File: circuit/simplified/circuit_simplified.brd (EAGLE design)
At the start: 100 x 80 mm, 78 parts

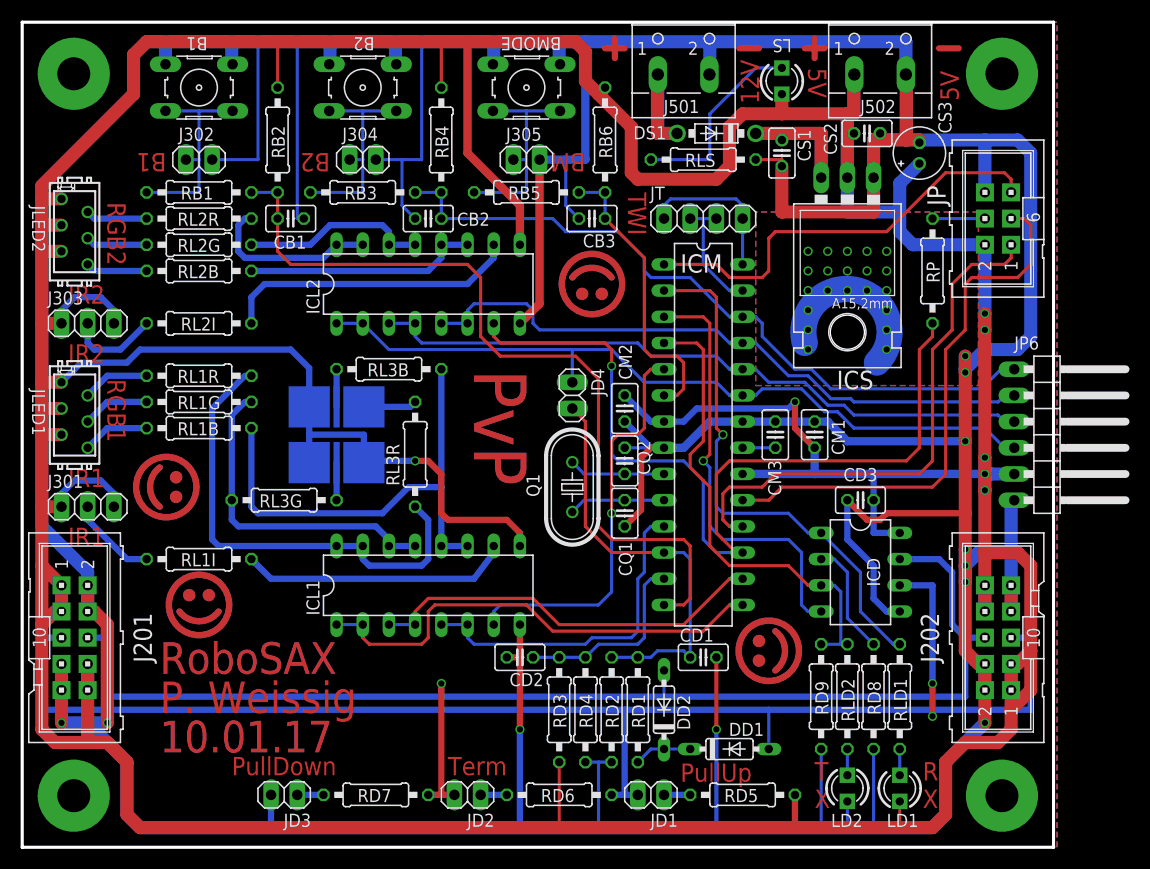
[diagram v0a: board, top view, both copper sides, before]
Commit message: updated circuit (added simplified version & minor bugfixes)
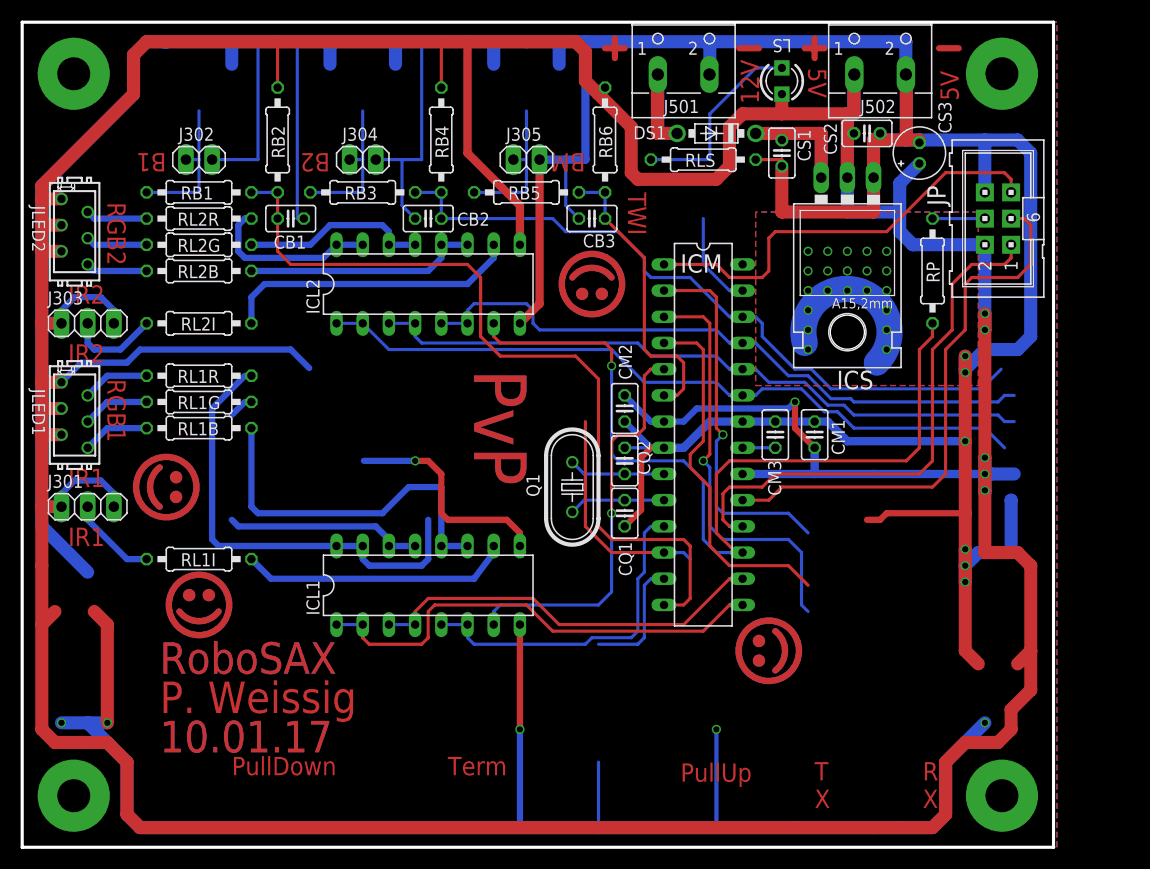
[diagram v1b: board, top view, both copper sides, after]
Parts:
- removed B1, B2, BMODE: (no value), switch-omron:B3F-10XX
- removed CD1, CD2: 100pF, rcl:C025-025X050
- removed CD3: 100nF, rcl:C025-025X050
- removed DD1, DD2: 1N4148, diode:DO35-7
- removed ICD: DRIVER_RS485, robo_ag:IC_DIL08
- removed J201, J202: (no value), robo_ag:STECKER_WANNE_10
- removed JD1, JD2, JD3, JD4: (no value), pinhead:1X02
- removed JP6: (no value), pinhead:1X06/90
- removed JT: (no value), pinhead:1X04
- removed LD1, LD2: (no value), robo_ag:LED_3MM
- removed LED3: LED_3X, robo_ag:LED_TOP_PLCC6
- removed RD1, RD6: 150, rcl:0207/10
- removed RD2: 100k, rcl:0207/10
- removed RD3, RD4: ?, rcl:0207/10
- removed RD5, RD7: 1k, rcl:0207/10
- removed RD8, RD9: 10k, rcl:0207/10
- removed RL3B, RL3G: 22, rcl:0207/10
- removed RL3R: 40,4, rcl:0207/10
- removed RLD1, RLD2: 300, rcl:0207/10
- LS: value (none) -> red
- RLS: value 300 -> 2k
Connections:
- removed net BUS_A: DD1.A, ICD.6, J201.5, J202.5, JD1.2, RD6.2
- removed net BUS_B: DD2.A, ICD.7, J201.6, J202.6, JD2.2, RD7.2
- removed net N$24: LED3.6, RL3R.2
- removed net N$25: LED3.2, RL3G.2
- removed net N$26: LED3.5, RL3B.2
- removed net N$31: JD1.1, RD5.1
- removed net N$32: ICD.2, RD8.1
- removed net N$33: JD2.1, RD6.1
- removed net N$34: LD1.K, RLD1.1
- removed net N$35: JD3.1, RD7.1
- removed net N$36: DD1.C, DD2.C, RD1.1
- removed net N$37: LD2.A, RLD2.2
- net +5V: no longer CD3.1, ICD.8, J201.1, J201.10, J201.3, J201.8, J202.1, J202.10, J202.3, J202.8, JP6.5, LD1.A, LED3.1, LED3.3, LED3.4, RD3.1, RD5.2
- net BTN2: no longer JP6.1
- net BUS_DETECT1: no longer CD1.1, JD4.2, RD1.2, RD2.2
- net BUS_DETECT2: no longer CD2.1, RD3.2, RD4.2
- net BUS_ENABLE: no longer ICD.3, RD9.1, RLD2.1
- net BUS_RX: no longer ICD.1, RLD1.2
- net BUS_TX: no longer ICD.4
- net GND: no longer B1.3, B1.4, B2.3, B2.4, BMODE.3, BMODE.4, CD1.2, CD2.2, CD3.2, ICD.5, J201.2, J201.4, J201.7, J201.9, J202.2, J202.4, J202.7, J202.9, JD3.2, JP6.6, LD2.K, RD2.1, RD4.1, RD8.2, RD9.2
- net LED1_B_OUT: no longer RL3B.1
- net LED1_G_OUT: no longer RL3G.1
- net LED1_R_OUT: no longer RL3R.1
- net LED2_B: no longer JP6.2
- net LED2_G: no longer JP6.3
- net LED2_R: no longer JD4.1, JP6.4
- net N$10: no longer BMODE.1, BMODE.2
- net N$4: no longer B1.1, B1.2
- net N$6: no longer B2.1, B2.2
- net TWI_SCL: no longer JT.1, JT.4
- net TWI_SDA: no longer JT.2, JT.3
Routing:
- net BUS_A: track 144.8 -> 0.00 mm, vias 2 -> 0
- net BUS_B: track 130.6 -> 0.00 mm, vias 1 -> 0
- net GND: track 675.6 -> 592.3 mm
- net +5V: track 608.5 -> 536.0 mm
- net BUS_DETECT1: track 41.1 -> 21.6 mm
- net BUS_RX: track 51.7 -> 36.1 mm
- net TWI_SCL: track 15.1 -> 0.00 mm
- net LED1_B_OUT: track 47.0 -> 35.6 mm
- net N$32: track 11.1 -> 0.00 mm
- net BUS_ENABLE: track 46.6 -> 35.5 mm
- net LED1_G_OUT: track 31.8 -> 21.6 mm
- net BUS_DETECT2: track 18.8 -> 12.0 mm
- net N$6: track 20.8 -> 14.2 mm
- net N$10: track 20.8 -> 14.2 mm
- net N$4: track 20.8 -> 14.2 mm
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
